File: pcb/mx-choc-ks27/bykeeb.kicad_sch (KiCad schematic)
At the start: 86 parts, among them J1 Conn_01x03_Female, J2 Conn_01x03_Female, M1 XIAO-BLE, M2 XIAO-BLE, SW1 SW_Push, SW10 SW_Push, SW11 SW_Push, SW12 SW_Push, SW13 SW_Push, SW14 SW_Push, SW15 SW_Push, SW16 SW_Push, SW17 SW_Push, SW18 SW_Push, SW19 SW_Push, SW2 SW_Push, SW20 SW_Push, SW21 SW_Push, SW22 SW_Push, SW23 SW_Push, SW24 SW_Push, SW25 SW_Push, SW26 SW_Push, SW27 SW_Push, SW28 SW_Push, SW29 SW_Push, SW3 SW_Push, SW30 SW_Push, SW31 SW_Push, SW32 SW_Push, SW33 SW_Push, SW34 SW_Push, SW35 SW_Push, SW36 SW_Push, SW37 SW_DPDT, SW38 SW_DPDT, SW4 SW_Push, SW5 SW_Push, SW6 SW_Push, SW7 SW_Push, SW8 SW_Push, SW9 SW_Push, U1 SW_Push, U2 SW_Push

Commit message: ready for prototype run
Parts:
- added H10, H7, H8, H9: Breakaway Tabs, fingerpunch:Breakaway_Tabs, symbol Mechanical:MountingHole
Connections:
- net col1: no longer M2.7 (D6)
- net col1_R: now also M2.7 (D6)
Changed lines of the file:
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@@
     )
   )
-  (global_label "col1" (shape input) (at 127.762 288.798 180) (fields_autoplaced)
+  (global_label "col1_R" (shape input) (at 127.762 288.798 180) (fields_autoplaced)
     (effects (font (size 1.27 1.27)) (justify right))
-    (property "Intersheetrefs" "${INTERSHEET_REFS}" (at 119.3297 288.8774 0)
+    (property "Intersheetrefs" "${INTERSHEET_REFS}" (at 119.1605 288.798 0)
       (effects (font (size 1.27 1.27)) (justify right) hide)
     )
@@
     )
   )
+  (symbol (lib_id "Mechanical:MountingHole") (at 34.29 192.278 0) (unit 1)
+    (in_bom yes) (on_board yes) (dnp no) (fields_autoplaced)
+    (property "Reference" "H10" (at 36.83 191.3695 0)
+      (effects (font (size 1.27 1.27)) (justify left))
+    )
+    (property "Value" "Breakaway Tabs" (at 36.83 194.1446 0)
+      (effects (font (size 1.27 1.27)) (justify left))
+    )
+    (property "Footprint" "fingerpunch:Breakaway_Tabs" (at 34.29 192.278 0)
+      (effects (font (size 1.27 1.27)) hide)
+    )
+    (property "Datasheet" "~" (at 34.29 192.278 0)
+      (effects (font (size 1.27 1.27)) hide)
+    )
+    (instances
+      (project "bykeeb"
+        (path "/61fe293f-6808-4b7f-9340-9aaac7054a97"
+          (reference "H10") (unit 1)
+        )
+      )
+    )
+  )
   (symbol (lib_id "Switch:SW_Push") (at 247.142 292.354 0) (unit 1)
     (in_bom yes) (on_board yes) (dnp no)
@@
     )
   )
+  (symbol (lib_id "Mechanical:MountingHole") (at 58.42 192.024 0) (unit 1)
+    (in_bom yes) (on_board yes) (dnp no) (fields_autoplaced)
+    (property "Reference" "H9" (at 60.96 191.1155 0)
+      (effects (font (size 1.27 1.27)) (justify left))
+    )
+    (property "Value" "Breakaway Tabs" (at 60.96 193.8906 0)
+      (effects (font (size 1.27 1.27)) (justify left))
+    )
+    (property "Footprint" "fingerpunch:Breakaway_Tabs" (at 58.42 192.024 0)
+      (effects (font (size 1.27 1.27)) hide)
+    )
+    (property "Datasheet" "~" (at 58.42 192.024 0)
+      (effects (font (size 1.27 1.27)) hide)
+    )
+    (instances
+      (project "bykeeb"
+        (path "/61fe293f-6808-4b7f-9340-9aaac7054a97"
+          (reference "H9") (unit 1)
+        )
+      )
+    )
+  )
   (symbol (lib_id "Switch:SW_Push") (at 280.162 319.024 0) (unit 1)
     (in_bom yes) (on_board yes) (dnp no)
@@
         (path "/61fe293f-6808-4b7f-9340-9aaac7054a97"
           (reference "SW27") (unit 1)
+        )
+      )
+    )
+  )
+  (symbol (lib_id "Mechanical:MountingHole") (at 34.29 185.674 0) (unit 1)
+    (in_bom yes) (on_board yes) (dnp no) (fields_autoplaced)
+    (property "Reference" "H8" (at 36.83 184.7655 0)
+      (effects (font (size 1.27 1.27)) (justify left))
+    )
+    (property "Value" "Breakaway Tabs" (at 36.83 187.5406 0)
+      (effects (font (size 1.27 1.27)) (justify left))
+    )
+    (property "Footprint" "fingerpunch:Breakaway_Tabs" (at 34.29 185.674 0)
+      (effects (font (size 1.27 1.27)) hide)
+    )
+    (property "Datasheet" "~" (at 34.29 185.674 0)
+      (effects (font (size 1.27 1.27)) hide)
+    )
+    (instances
+      (project "bykeeb"
+        (path "/61fe293f-6808-4b7f-9340-9aaac7054a97"
+          (reference "H8") (unit 1)
         )
       )
@@
         )
       )
+    )
+  )
+  (symbol (lib_id "Mechanical:MountingHole") (at 58.42 185.42 0) (unit 1)
+    (in_bom yes) (on_board yes) (dnp no) (fields_autoplaced)
+    (property "Reference" "H7" (at 60.96 184.5115 0)
+      (effects (font (size 1.27 1.27)) (justify left))
+    )
+    (property "Value" "Breakaway Tabs" (at 60.96 187.2866 0)
+      (effects (font (size 1.27 1.27)) (justify left))
+    )
+    (property "Footprint" "fingerpunch:Breakaway_Tabs" (at 58.42 185.42 0)
+      (effects (font (size 1.27 1.27)) hide)
+    )
+    (property "Datasheet" "~" (at 58.42 185.42 0)
+      (effects (font (size 1.27 1.27)) hide)
+    )
+    (instances
+      (project "bykeeb"
+        (path "/61fe293f-6808-4b7f-9340-9aaac7054a97"
+          (reference "H7") (unit 1)
+        )
+      )

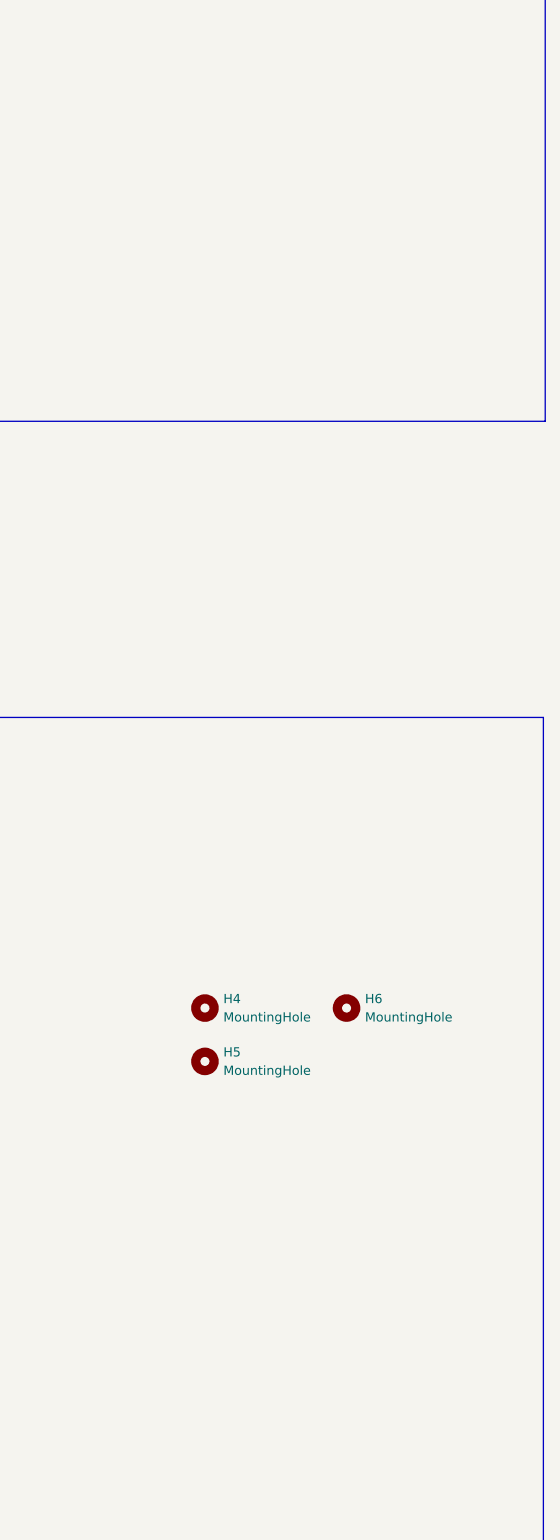
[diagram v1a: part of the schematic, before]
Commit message: mounting holes on each side in case we want to try out vik trackpoint support
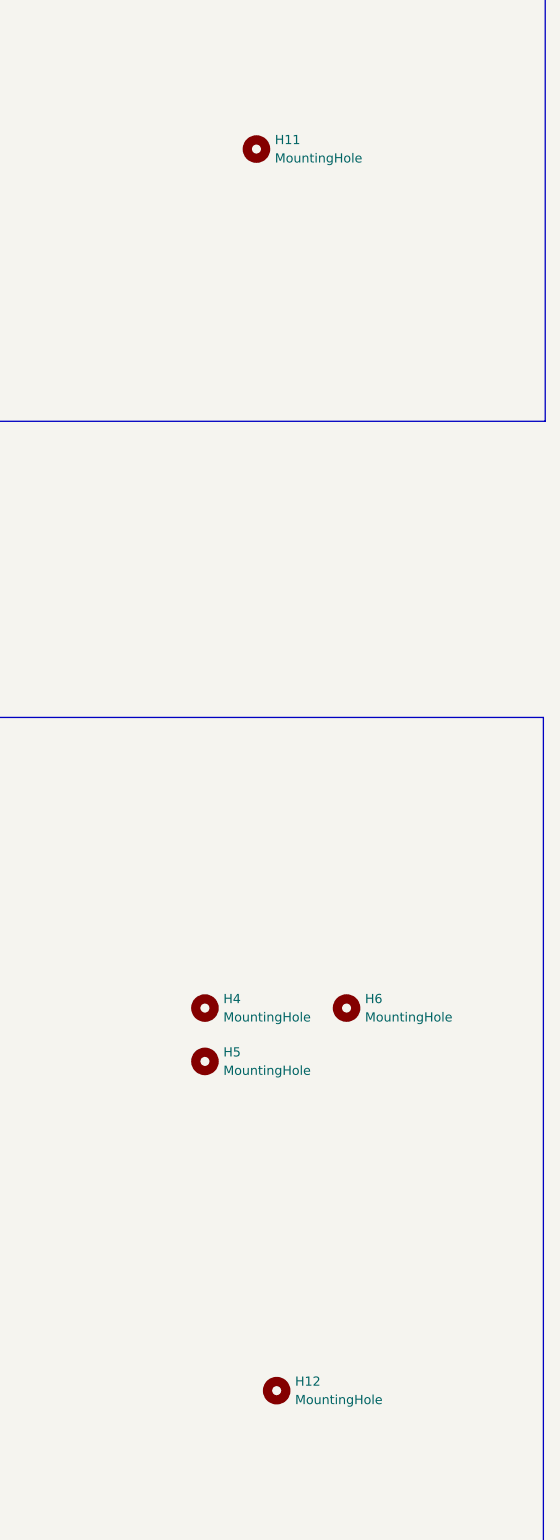
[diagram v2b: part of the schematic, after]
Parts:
- added H11, H12: MountingHole, MountingHole:MountingHole_3.2mm_M3, symbol Mechanical:MountingHole
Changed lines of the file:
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@@
+    )
+  )
+  (symbol (lib_id "Mechanical:MountingHole") (at 327.914 304.8 0) (unit 1)
+    (in_bom yes) (on_board yes) (dnp no) (fields_autoplaced)
+    (property "Reference" "H12" (at 330.454 303.53 0)
+      (effects (font (size 1.27 1.27)) (justify left))
+    )
+    (property "Value" "MountingHole" (at 330.454 306.07 0)
+      (effects (font (size 1.27 1.27)) (justify left))
+    )
+    (property "Footprint" "MountingHole:MountingHole_3.2mm_M3" (at 327.914 304.8 0)
+      (effects (font (size 1.27 1.27)) hide)
+    )
+    (property "Datasheet" "~" (at 327.914 304.8 0)
+      (effects (font (size 1.27 1.27)) hide)
+    )
+    (instances
+      (project "bykeeb"
+        (path "/61fe293f-6808-4b7f-9340-9aaac7054a97"
+          (reference "H12") (unit 1)
+        )
+      )
     )
   )
@@
         )
       )
+    )
+  )
+  (symbol (lib_id "Mechanical:MountingHole") (at 325.12 133.35 0) (unit 1)
+    (in_bom yes) (on_board yes) (dnp no) (fields_autoplaced)
+    (property "Reference" "H11" (at 327.66 132.08 0)
+      (effects (font (size 1.27 1.27)) (justify left))
+    )
+    (property "Value" "MountingHole" (at 327.66 134.62 0)
+      (effects (font (size 1.27 1.27)) (justify left))
+    )
+    (property "Footprint" "MountingHole:MountingHole_3.2mm_M3" (at 325.12 133.35 0)
+      (effects (font (size 1.27 1.27)) hide)
+    )
+    (property "Datasheet" "~" (at 325.12 133.35 0)
+      (effects (font (size 1.27 1.27)) hide)
+    )
+    (instances
+      (project "bykeeb"
+        (path "/61fe293f-6808-4b7f-9340-9aaac7054a97"
+          (reference "H11") (unit 1)
+        )
+      )
